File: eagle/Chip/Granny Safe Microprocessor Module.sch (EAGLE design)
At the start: 33 parts, among them IC1 MCP604SL, J1 3x4 Keypad, Q3 TRANS_NPN-MMBTA42, U1 328P, Y1 16MHz

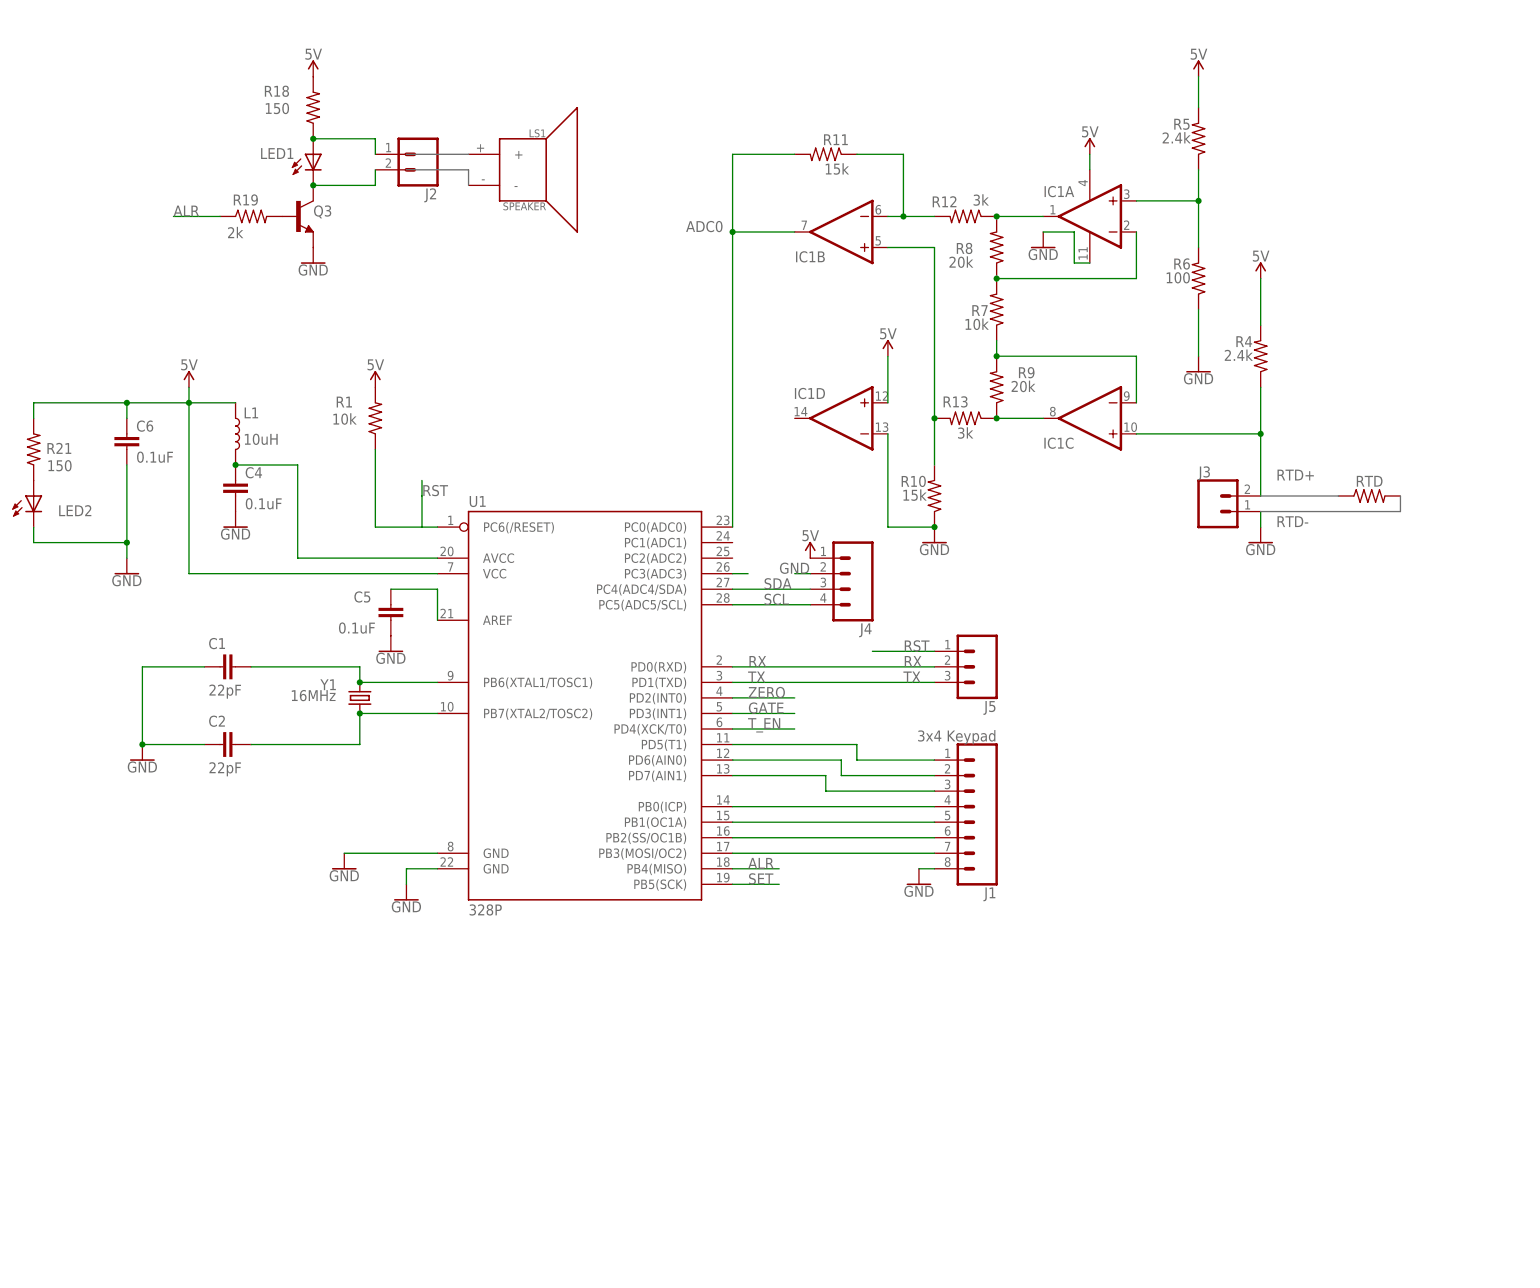
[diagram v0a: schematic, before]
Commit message: Updated uc schematic
dont forget to think about test points
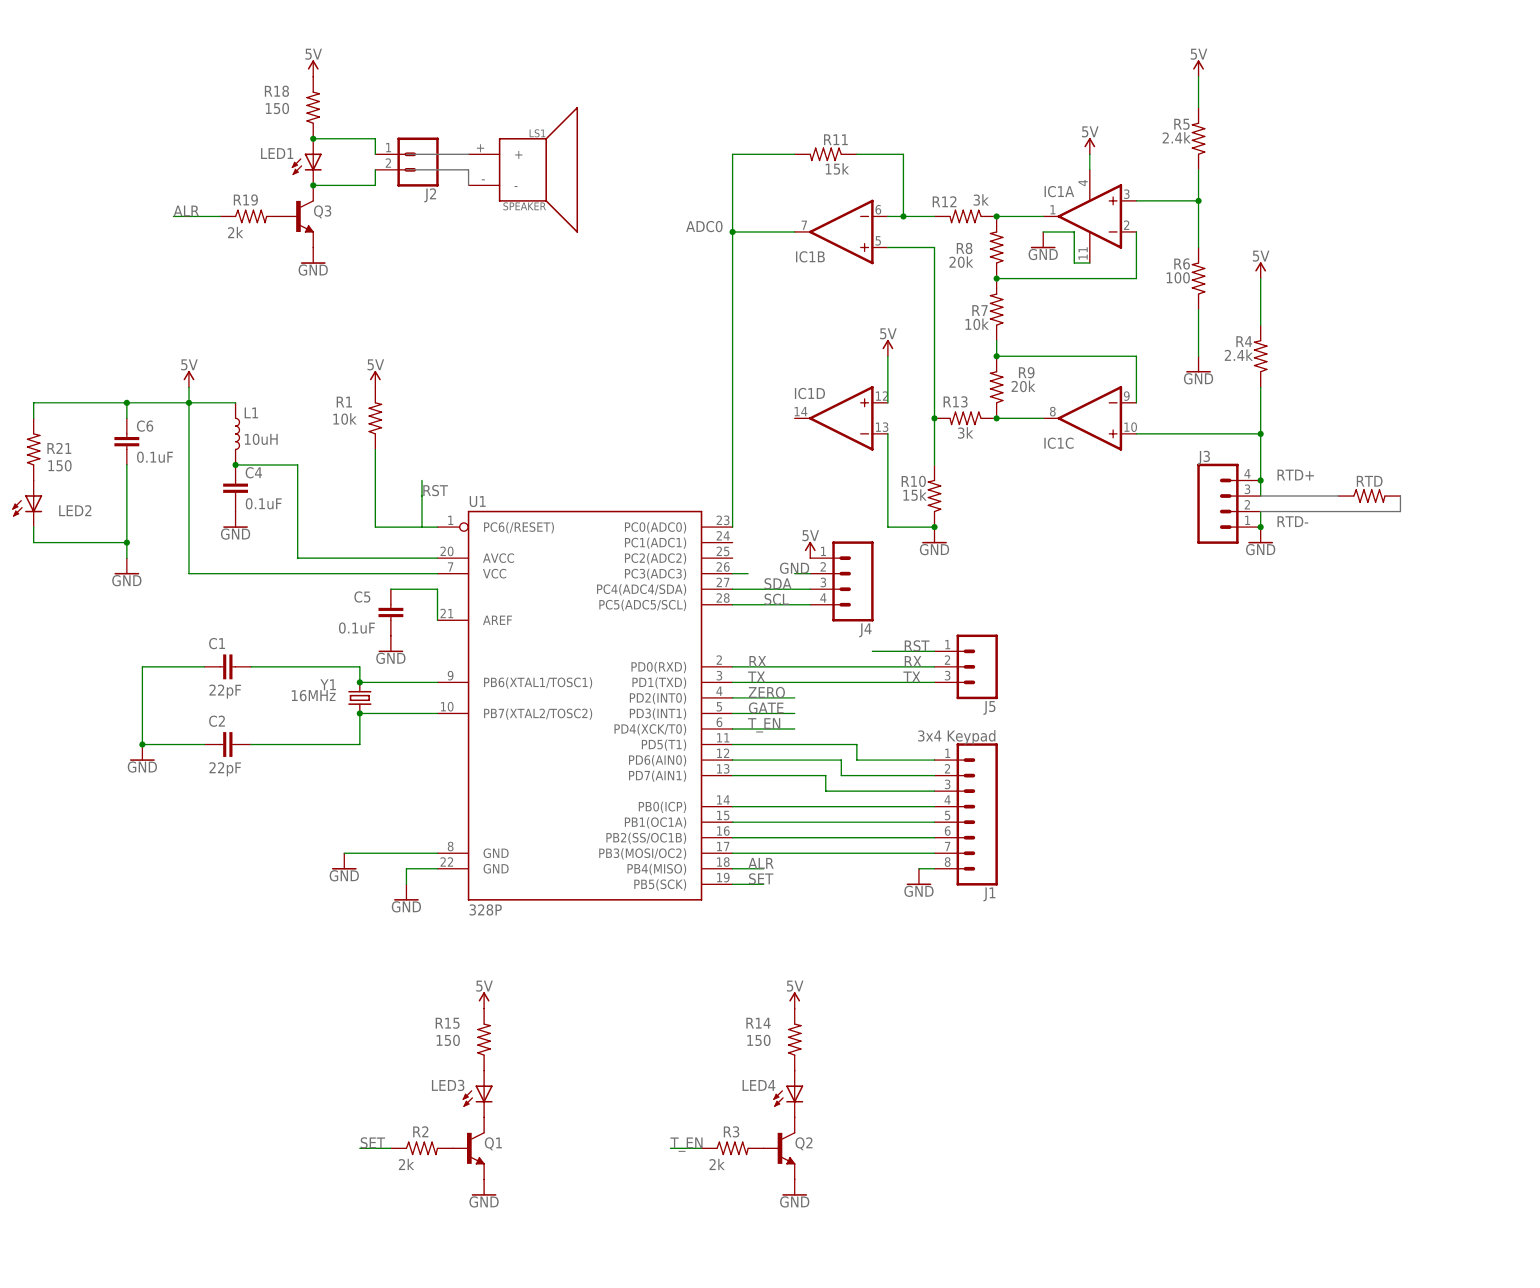
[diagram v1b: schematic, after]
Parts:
- added LED3, LED4: (no value), adafruit:LED5MM
- added Q1, Q2: TRANS_NPN-MMBTA42, SparkFun-DiscreteSemi:TRANS_NPN-MMBTA42
- added R14, R15: 150, adafruit:R-US_R0603
- added R2, R3: 2k, adafruit:R-US_R0603
- J3: value (none) -> SCREW-4; device SparkFun-Connectors:CONN_025MM -> ece:SCREW-4
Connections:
- new net N$12: Q1.B, R2.2
- new net N$14: Q2.B, R3.2
- new net N$17: LED3.A, R15.1
- new net N$18: LED4.A, R14.1
- new net N$19: LED4.C, Q2.C
- new net N$20: LED3.C, Q1.C
- net 5V: now also R14.2, R15.2
- net GND: now also J3.2, Q1.E, Q2.E
- net N$13: now also J3.3, J3.4; no longer J3.2
- net SET: now also R2.1
- net T_EN: now also R3.1

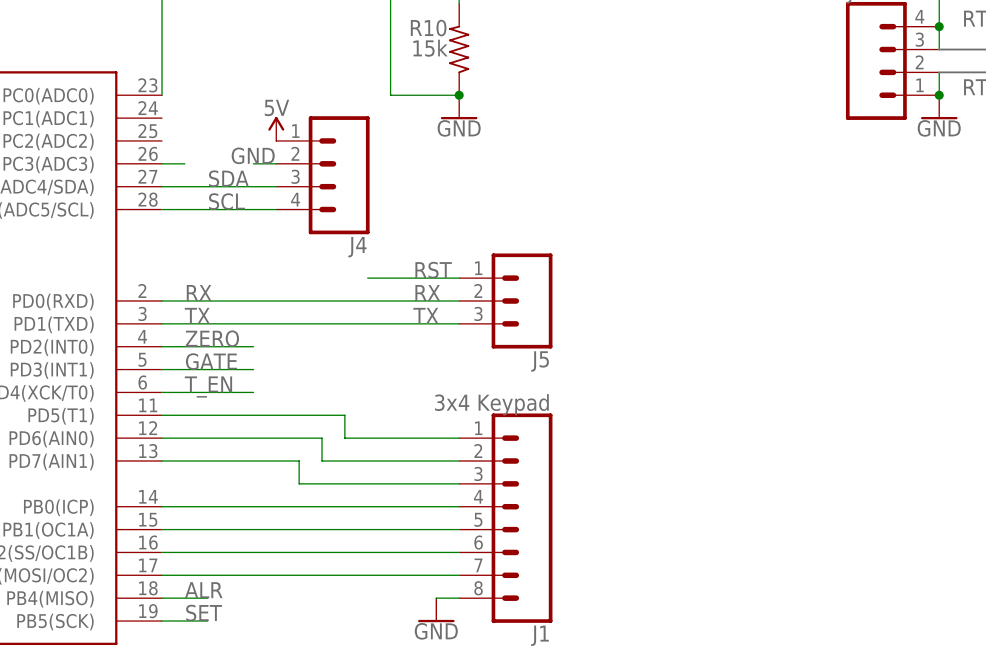
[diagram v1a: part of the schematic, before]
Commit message: PWR SUP, all but test point
need a way to hook up the resistor too
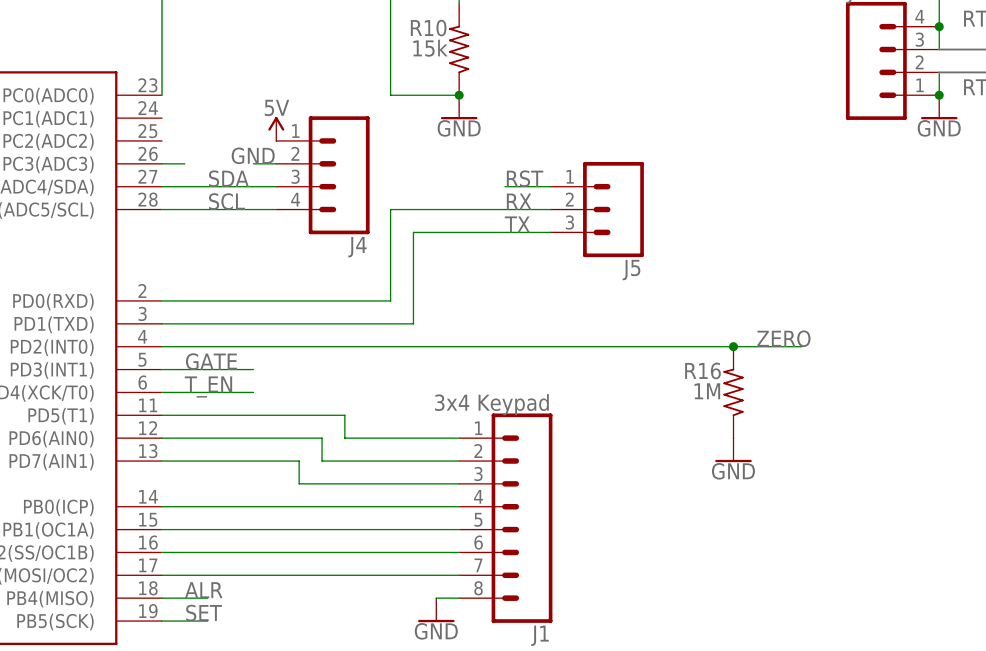
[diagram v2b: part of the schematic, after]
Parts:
- added R16: 1M, resistor:R-US_R0603
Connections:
- net GND: now also R16.1
- net ZERO: now also R16.2
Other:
- moved on the sheet: J5

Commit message: More updates to schematics
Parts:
- added J6: FEMALE 2x3, SparkFun-Connectors:CONN_03X2FEMALE
- added R17: 5k, resistor:R-US_R0603
- added VR1: 10k, SparkFun-Resistors:TRIMPOT-SMD-3MM-CLOSED-1/8W-20%
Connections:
- new net N$21: R17.2, VR1.CW, VR1.WIPER
- net 5V: now also J6.1, J6.3, J6.5
- net GND: now also J6.2, J6.4, J6.6; no longer J1.8
- net N$24: now also R17.1
- net N$26: now also VR1.CCW
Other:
- note added: "COMBINE"
- note added: "HEADERS"
- note added: "Test points"
- moved on the sheet: IC1A, R12, R4, R5, R6, R7, R8

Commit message: Put both schematics together
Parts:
- removed Y1: 16MHz, SparkFun-Clocks:CRYSTAL-16MHZPTH-HC49US
- added TP1, TP2, TP3, TP4, TP5, TP6, TP7: (no value), SparkFun-Connectors:CONN_01
- added XTAL: 16MHz, SparkFun-Clocks:CRYSTAL-16MHZPTH-HC49US
- J4: value (none) -> i2c_16x2
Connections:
- removed net N$50: U1.PC3(ADC3)
- net 5V: now also TP4.1
- net ADC0: now also TP2.1
- net ALR: now also TP7.1
- net GND: now also TP3.1
- net N$1: now also XTAL.2; no longer Y1.2
- net N$2: now also XTAL.1; no longer Y1.1
- net SET: now also TP5.1
- net T_EN: now also TP6.1
- net ZERO: now also TP1.1
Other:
- note removed: "ADC0"
- moved on the sheet: C1, C2, C4, C5, C6, IC1A, IC1B, IC1C, IC1D, J1, J2, J3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
